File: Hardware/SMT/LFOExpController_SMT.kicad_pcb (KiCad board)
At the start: 2 copper layers, 87.2 x 85.3 mm, 54 parts

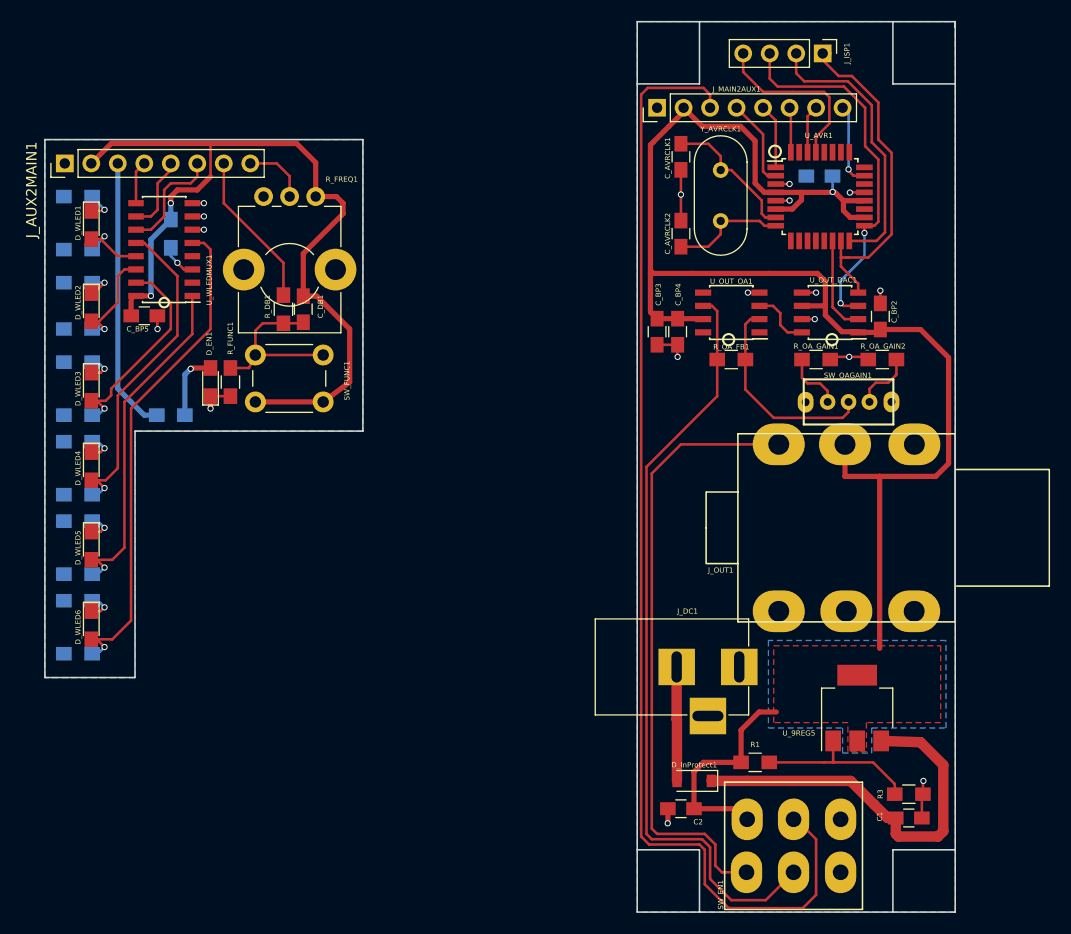
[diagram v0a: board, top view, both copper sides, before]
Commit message: Completed Board Layout
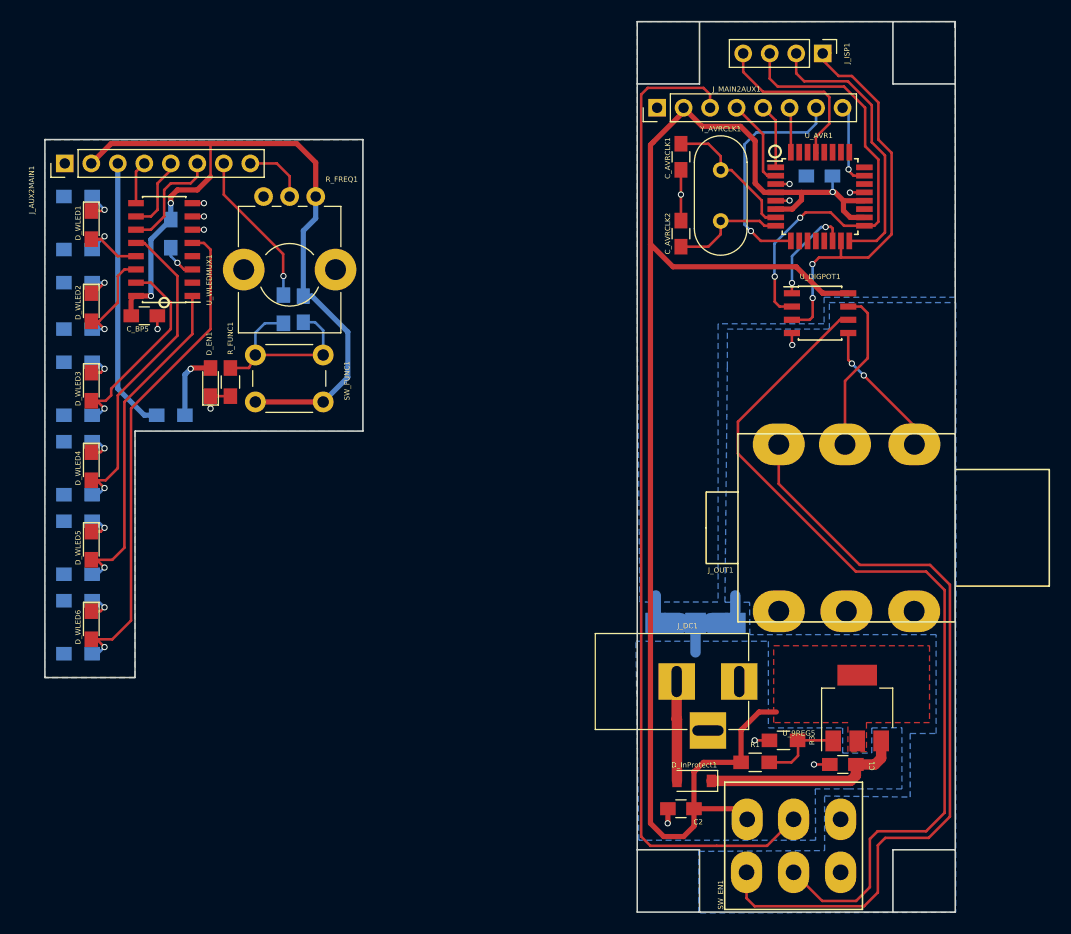
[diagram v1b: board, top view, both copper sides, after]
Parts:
- removed C_BP2, C_BP4: 100nF, Capacitors_SMD:C_0805_HandSoldering
- removed C_BP3: 1uF, Capacitors_SMD:C_0805_HandSoldering
- removed R_OA_FB1: 10K, Resistors_SMD:R_0805_HandSoldering
- removed R_OA_GAIN1: 5K6, Resistors_SMD:R_0805_HandSoldering
- removed R_OA_GAIN2: 12K, Resistors_SMD:R_0805_HandSoldering
- removed SW_OAGAIN1: SW_SPDT, C&K_8_6mm_SPDT_ONON:C&K_8_6mm_SPDT_ONON
- removed U_OUT_DAC1: MCP4921, Housings_SOIC:SOIC-8_3.9x4.9mm_Pitch1.27mm
- removed U_OUT_OA1: MCP601-xSN, Housings_SOIC:SOIC-8_3.9x4.9mm_Pitch1.27mm
- added JP_GND1: Jumper_NC_Dual, NetTie-II_SMD_FakeConnected:NetTie-II_SMD_GraphicallyConnected, B.Cu at (130.9, 110.1)
- added U_DIGPOT1: _MCP41050, Housings_SOIC:SOIC-8_3.9x4.9mm_Pitch1.27mm, F.Cu at (142.9, 80.4)
- C_DB1, R_DB1: moved to B.Cu
- J_AUX2MAIN1: value Conn_01x08 -> _Conn_01x08
- R_FUNC1: value 10K -> 1K
- moved R3 13.1 mm to (139.4, 121.3), turned to 180 degrees
- moved C1 8.14 mm to (145.1, 123.6), turned to 0 degrees
- moved J_DC1 1.40 mm to (135.1, 115.7)
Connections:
- net /SWEN_OUT renamed /TIP_SIGOUT
- C_AVRCLK1 pad 1: /GND -> /DGND
- C_AVRCLK2 pad 1: /GND -> /DGND
- C_BP1 pad 2: /GND -> /DGND
- J_MAIN2AUX1 pad 1: /GND -> /DGND
- J_OUT1 pad 2: /+5V -> /RING_SIGOUT
- J_OUT1 pad 3: /GND -> /SLEEVE_SIGOUT
- SW_EN1 pad 5: /OA_SWEN -> Net-(SW_EN1-Pad5)
- U_AVR1 pad 21: /GND -> /DGND
- U_AVR1 pad 3: /GND -> /DGND
- U_AVR1 pad 30: /SW_FUNC -> Net-(U_AVR1-Pad30)
- U_AVR1 pad 5: /GND -> /DGND
- U_AVR1 pad 9: Net-(U_AVR1-Pad9) -> /SW_FUNC
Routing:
- net Net-(SW_EN1-Pad5): track 0.00 -> 86.7 mm
- net /OA_SWEN: track 74.9 -> 0.00 mm
- net Net-(R_OA_FB1-Pad2): track 20.2 -> 0.00 mm
- net /9V: track 38.8 -> 19.6 mm
- net /GND: track 25.7 -> 7.63 mm, vias 12 -> 3
- net /TIP_SIGOUT: track 59.4 -> 76.7 mm
- net /SW_FUNC: track 4.89 -> 22.0 mm, vias 0 -> 1
- net /RING_SIGOUT: track 0.00 -> 15.7 mm
- net /PWRSW: track 109.9 -> 95.8 mm
- net /SLEEVE_SIGOUT: track 0.00 -> 13.3 mm, vias 0 -> 2
- net /DGND: track 0.00 -> 11.6 mm, vias 0 -> 4
- net /REG_ADJ: track 15.9 -> 8.03 mm
- net /SCK: track 35.8 -> 43.5 mm
- net /MOSI: track 33.0 -> 39.1 mm, vias 0 -> 2
- net Net-(R_OA_GAIN1-Pad2): track 6.04 -> 0.00 mm
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- added copper zone on B.Cu, net /AGND
- added copper zone on B.Cu, net /DGND

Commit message: Generated GERBERS
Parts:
- added REF**: VIA-0.6mm, VIA_0_6mm:VIA_0_6mm, B.Cu at (149.2, 113.2)
- added REF**: VIA-0.6mm, VIA_0_6mm:VIA_0_6mm, B.Cu at (152.1, 116.0)
- added REF**: VIA-0.6mm, VIA_0_6mm:VIA_0_6mm, B.Cu at (150.7, 116.0)
- added REF**: VIA-0.6mm, VIA_0_6mm:VIA_0_6mm, B.Cu at (152.1, 114.6)
- added REF**: VIA-0.6mm, VIA_0_6mm:VIA_0_6mm, B.Cu at (150.7, 114.6)
- added REF**: VIA-0.6mm, VIA_0_6mm:VIA_0_6mm, B.Cu at (152.1, 113.2)
- added REF**: VIA-0.6mm, VIA_0_6mm:VIA_0_6mm, B.Cu at (150.7, 113.2)
- added REF**: VIA-0.6mm, VIA_0_6mm:VIA_0_6mm, B.Cu at (142.2, 118.8)
- added REF**: VIA-0.6mm, VIA_0_6mm:VIA_0_6mm, B.Cu at (140.8, 118.8)
- added REF**: VIA-0.6mm, VIA_0_6mm:VIA_0_6mm, B.Cu at (139.4, 118.8)
- added REF**: VIA-0.6mm, VIA_0_6mm:VIA_0_6mm, B.Cu at (142.2, 117.4)
- added REF**: VIA-0.6mm, VIA_0_6mm:VIA_0_6mm, B.Cu at (147.8, 113.2)
- added REF**: VIA-0.6mm, VIA_0_6mm:VIA_0_6mm, B.Cu at (140.8, 117.4)
- added REF**: VIA-0.6mm, VIA_0_6mm:VIA_0_6mm, B.Cu at (139.4, 117.4)
- added REF**: VIA-0.6mm, VIA_0_6mm:VIA_0_6mm, B.Cu at (142.2, 116.0)
- added REF**: VIA-0.6mm, VIA_0_6mm:VIA_0_6mm, B.Cu at (140.8, 116.0)
- added REF**: VIA-0.6mm, VIA_0_6mm:VIA_0_6mm, B.Cu at (139.4, 116.0)
- added REF**: VIA-0.6mm, VIA_0_6mm:VIA_0_6mm, B.Cu at (142.2, 114.6)
- added REF**: VIA-0.6mm, VIA_0_6mm:VIA_0_6mm, B.Cu at (140.8, 114.6)
- added REF**: VIA-0.6mm, VIA_0_6mm:VIA_0_6mm, B.Cu at (139.4, 114.6)
- added REF**: VIA-0.6mm, VIA_0_6mm:VIA_0_6mm, B.Cu at (142.2, 113.2)
- added REF**: VIA-0.6mm, VIA_0_6mm:VIA_0_6mm, B.Cu at (140.8, 113.2)
- added REF**: VIA-0.6mm, VIA_0_6mm:VIA_0_6mm, B.Cu at (146.4, 113.2)
- added REF**: VIA-0.6mm, VIA_0_6mm:VIA_0_6mm, B.Cu at (139.4, 113.2)
- added REF**: VIA-0.6mm, VIA_0_6mm:VIA_0_6mm, B.Cu at (145.0, 113.2)
- added REF**: VIA-0.6mm, VIA_0_6mm:VIA_0_6mm, B.Cu at (143.6, 113.2)
- added REF**: VIA-0.6mm, VIA_0_6mm:VIA_0_6mm, B.Cu at (152.1, 118.8)
- added REF**: VIA-0.6mm, VIA_0_6mm:VIA_0_6mm, B.Cu at (150.7, 118.8)
- added REF**: VIA-0.6mm, VIA_0_6mm:VIA_0_6mm, B.Cu at (152.1, 117.4)
- added REF**: VIA-0.6mm, VIA_0_6mm:VIA_0_6mm, B.Cu at (150.7, 117.4)
- moved C_DB1 27.4 mm to (118.3, 68.7)
- moved D_EN1 27.4 mm to (109.4, 75.7)
- moved R_DB1 27.4 mm to (116.4, 68.7)
- moved R_FUNC1 27.4 mm to (111.4, 75.7)
- moved R_WLEDA2 27.4 mm to (96.7, 70.6)
- moved R_WLEDA4 27.4 mm to (96.7, 86.5)
- moved SW_FUNC1 27.4 mm to (120.2, 77.6)
- moved J_AUX2MAIN1 27.4 mm to (95.5, 54.7)
- moved R_FREQ1 27.4 mm to (114.5, 57.9)
- moved R_WLEDA1 27.4 mm to (96.7, 63.0)
- moved R_WLEDB1 27.4 mm to (96.7, 57.9)
- moved U_WLEDMUX1 27.4 mm to (105.0, 63.0)
- moved C_BP5 27.4 mm to (103.1, 69.3)
- moved R_EN1 27.4 mm to (105.6, 78.9)
- moved R_MUXIN1 27.4 mm to (105.6, 61.5)
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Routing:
- net /WAVELED1: track 8.08 -> 13.6 mm
- net /WAVELED2: track 10.6 -> 15.9 mm
- net /WAVELED3: track 20.5 -> 25.8 mm
- net /WAVELED4: track 32.1 -> 37.4 mm
- net /WAVELED6: track 48.3 -> 53.6 mm
- net /WAVELED5: track 33.5 -> 38.8 mm
- net Net-(D_WLED1-Pad1): track 3.06 -> 5.84 mm
- net Net-(D_WLED6-Pad1): track 2.87 -> 5.64 mm
- net Net-(D_WLED3-Pad1): track 2.87 -> 5.64 mm
- net Net-(D_WLED5-Pad1): track 2.87 -> 5.64 mm
- net Net-(D_WLED4-Pad1): track 2.87 -> 5.64 mm
- net Net-(D_WLED2-Pad1): track 2.87 -> 5.38 mm
- added copper zone on B.Cu, net /+5V
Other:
- board size 87.2 x 85.3 mm -> 62.3 x 85.3 mm
- board text added: "LFO EXP Controller Rev2 by Chris Sutton 102018"
- board text added: "LFO Expression Controller"
- board text added: "Rev2 By Chris Sutton 102018"

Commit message: Revision3 update
- Added ground to Jack sleeve pin
- Corrected SW_FUNC circuit
- Removed R_WLEDB LEDS
- Modified firmware from eight wavepatterns to six, to allign with Hardware (Sine, Triangle, RampUp, Step4, Square, Pulse)
- Created R3 documentation
- Created new GERBERS
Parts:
- removed R_WLEDB1, R_WLEDB2, R_WLEDB3, R_WLEDB4, R_WLEDB5, R_WLEDB6: 1K, Resistors_SMD:R_0805_HandSoldering
- R_EN1: value R -> 1K; moved to F.Cu
- moved R_EN1 3.96 mm to (109.3, 77.5), turned to 180 degrees
- moved R_FUNC1 2.86 mm to (109.3, 73.7), turned to 0 degrees
- moved D_WLED1 1.76 mm to (96.8, 60.1), turned to 0 degrees
- moved D_WLED2 1.70 mm to (96.8, 67.8), turned to 0 degrees
- moved D_WLED3 1.65 mm to (96.8, 75.6), turned to 0 degrees
- moved D_WLED4 1.61 mm to (96.8, 83.3), turned to 0 degrees
- moved D_WLED5 1.57 mm to (96.8, 91.1), turned to 0 degrees
- moved D_WLED6 1.55 mm to (96.8, 98.8), turned to 0 degrees
- moved C_DB1 0.50 mm to (117.9, 68.6)
- moved R_DB1 0.34 mm to (116.2, 68.5)
- moved R_WLEDA2 0.26 mm to (96.8, 70.9)
- moved D_EN1 0.16 mm to (109.3, 75.6), turned to 180 degrees
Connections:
- D_WLED1 pad 1: Net-(D_WLED1-Pad1) -> /AUXGND
- D_WLED2 pad 1: Net-(D_WLED2-Pad1) -> /AUXGND
- D_WLED3 pad 1: Net-(D_WLED3-Pad1) -> /AUXGND
- D_WLED4 pad 1: Net-(D_WLED4-Pad1) -> /AUXGND
- D_WLED5 pad 1: Net-(D_WLED5-Pad1) -> /AUXGND
- D_WLED6 pad 1: Net-(D_WLED6-Pad1) -> /AUXGND
- J_OUT1 pad 3: /SLEEVE_SIGOUT -> /AGND
- U_DIGPOT1 pad 5: /SLEEVE_SIGOUT -> /AGND
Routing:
- net /AGND: track 3.82 -> 17.1 mm, vias 1 -> 3
- net /SLEEVE_SIGOUT: track 13.3 -> 0.00 mm, vias 2 -> 0
- net /AUXGND: track 7.70 -> 20.9 mm, vias 5 -> 11
- net /WAVELED5: track 38.8 -> 32.3 mm
- net /WAVELED4: track 37.4 -> 31.2 mm
- net /PWRLED: track 26.4 -> 32.6 mm, vias 0 -> 1
- net Net-(D_WLED1-Pad1): track 5.84 -> 0.00 mm, vias 1 -> 0
- net /WAVELED6: track 53.6 -> 47.8 mm
- net Net-(D_WLED6-Pad1): track 5.64 -> 0.00 mm, vias 1 -> 0
- net Net-(D_WLED3-Pad1): track 5.64 -> 0.00 mm, vias 1 -> 0
- net Net-(D_WLED5-Pad1): track 5.64 -> 0.00 mm, vias 1 -> 0
- net Net-(D_WLED4-Pad1): track 5.64 -> 0.00 mm, vias 1 -> 0
- net Net-(D_WLED2-Pad1): track 5.38 -> 0.00 mm, vias 1 -> 0
- net /WAVELED3: track 25.8 -> 20.5 mm
- net /WAVELED1: track 13.6 -> 8.57 mm
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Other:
- board text added: "LFO EXP Controller Rev3 by Chris Sutton 122018"
- board text added: "MOSI MISO SCK RST"
- board text added: "RST SCK MISO MOSI"
- board text added: "Rev3 By Chris Sutton 122018"
- board text removed: "LFO EXP Controller Rev2 by Chris Sutton 102018"
- board text removed: "Rev2 By Chris Sutton 102018"
